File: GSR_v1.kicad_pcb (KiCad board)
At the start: 2 copper layers, 33.4 x 36 mm, 71 parts, among them IC1 AD5242BRUZ1M, J1 Micro_SD_Card_Det, P1 CONN_2, P2 CONN_2, P3 CONN_2, P4 CONN_2, Q1 DMP21D5UFB4-7B, U1 TPS63001, U2 LM324N, U3 NRF528XX-QFAA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

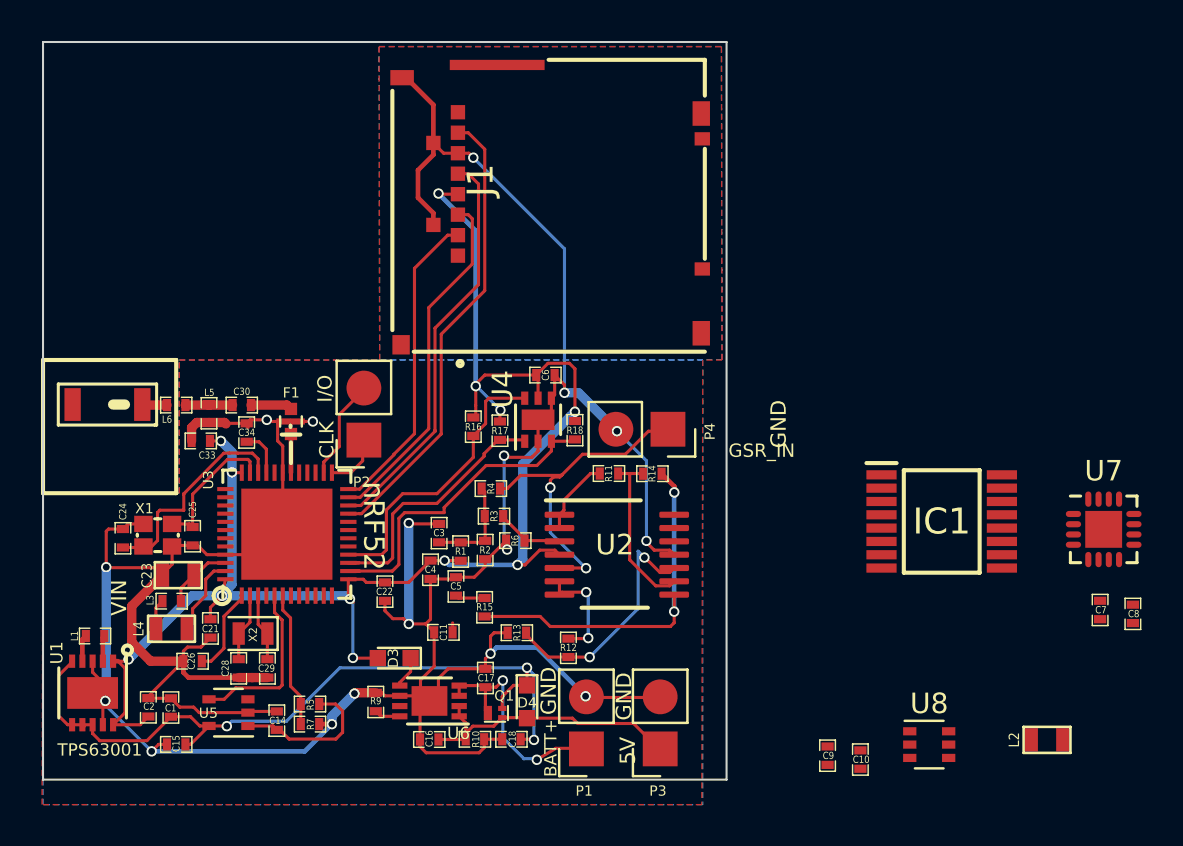
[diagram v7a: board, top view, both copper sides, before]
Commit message: Added switch and arranged and routed PCB.
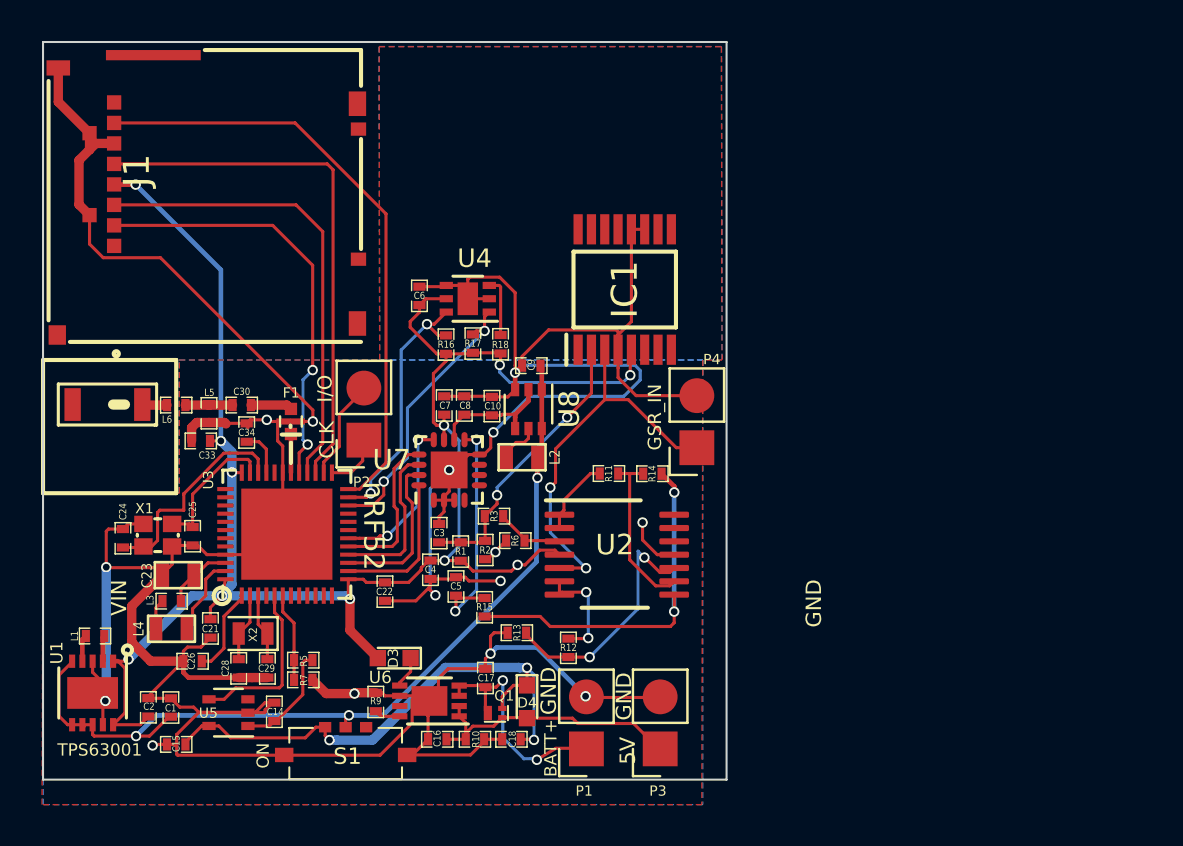
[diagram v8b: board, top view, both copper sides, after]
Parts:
- removed C11: 1uF, SM0402
- removed R4: 200k, SM0402
- added S1: SSAJ120100, SSAJ120100:SSAJ120100, F.Cu at (279.7, 143.4)
- moved C8 34.2 mm to (286.5, 127.7)
- moved C7 33.5 mm to (285.5, 127.7)
- moved U7 32.1 mm to (285.7, 130.9), turned to 90 degrees
- moved L2 29.1 mm to (289.3, 130.2), turned to 0 degrees
- moved U8 25.5 mm to (289.6, 127.9), turned to 270 degrees
- moved C10 24.9 mm to (287.8, 127.8)
- moved C9 23.9 mm to (289.7, 125.8), turned to 180 degrees
- moved IC1 19.2 mm to (294.3, 122.1), turned to 90 degrees
- moved J1 16.8 mm to (266.2, 110.4)
- moved C6 7.26 mm to (284.3, 122.4), turned to 270 degrees
- moved U4 6.83 mm to (286.6, 122.5), turned to 180 degrees
- moved R18 5.55 mm to (288.2, 124.7), turned to 270 degrees
- moved R17 4.45 mm to (286.9, 124.7), turned to 270 degrees
- moved R16 4.22 mm to (285.6, 124.7), turned to 270 degrees
- moved R7 2.18 mm to (278.6, 141.1)
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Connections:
- C15 pad 1: VCC -> /LOAD_IN
- C18 pad 2: VCC -> /LOAD_IN
- D4 pad 1: VCC -> /LOAD_IN
- Q1 pad 3: VCC -> /LOAD_IN
- R18 pad 1: /ALERT -> /TMP_ALERT
- U3 pad 14: /ALERT -> /SPI_~CS
- U3 pad 15: /TMP_SCL -> /SPI_SCLK
- U3 pad 16: /TMP_SDA -> /DIN
- U3 pad 17: Net-(U3-Pad17) -> /DOUT
- U3 pad 18: Net-(U3-Pad18) -> /~DRDY
- U3 pad 21: /DAT0_MISO -> Net-(U3-Pad21)
- U3 pad 22: /uSD_CLK -> /TMP_SCL
- U3 pad 23: /CMD_MOSI -> /TMP_SDA
- U3 pad 24: /DAT3_CS -> /DAT0_MISO
- U3 pad 27: Net-(U3-Pad27) -> /uSD_CLK
- U3 pad 28: Net-(U3-Pad28) -> /CMD_MOSI
- U3 pad 29: Net-(U3-Pad29) -> /DAT3_CS
- U4 pad 3: /ALERT -> /TMP_ALERT
- U5 pad 5: VCC -> /LOAD_IN
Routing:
- net DGND: track 187.4 -> 228.4 mm, vias 17 -> 15
- net /LOAD_IN: track 0.00 -> 26.7 mm, vias 0 -> 3
- net /ALERT: track 15.6 -> 0.00 mm
- net /RT_1: track 0.00 -> 13.8 mm, vias 0 -> 2
- net DVDD: track 80.3 -> 90.7 mm, vias 12 -> 11
- net /ADC_AIN0: track 1.45 -> 11.6 mm, vias 0 -> 2
- net /~DRDY: track 0.00 -> 8.04 mm, vias 0 -> 2
- net /SPI_SCLK: track 0.00 -> 7.80 mm
- net /DIN: track 0.00 -> 7.79 mm
- net /DOUT: track 0.00 -> 7.60 mm
- net /DAT0_MISO: track 22.6 -> 29.9 mm
- net /SPI_~CS: track 0.00 -> 7.29 mm
- net AVDD: track 0.00 -> 6.11 mm
- net /uSD_CLK: track 20.0 -> 25.9 mm
- net VCC: track 37.3 -> 43.0 mm
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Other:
- board text added: "ON"
